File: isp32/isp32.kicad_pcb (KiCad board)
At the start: 2 copper layers, 58 parts, among them J1 BAT1, J3 USB_C_Receptacle_USB2.0, J6 F0, J7 F1, Q1 BSS138, Q2 BSS138, Q3 IRLML6402, Q4 BSS138, Q5 IRLML6402, Q6 S8050, Q7 S8050, Q8 S8050, U1 ICE40HX8K-BG121, U10 BMP280, U11 MPU-9250, U12 CH340C, U2 USBLC6-2SC6, U3 ESP32-WROOM-32U, U4 AMS1117-3.3, U5 MP2303ADN, U6 MIC5504-1.2YM5, U7 NEO-XM, U8 AT25SF081-SSHD-X, U9 RFM98W-315S2, X1 ASE-25MHz

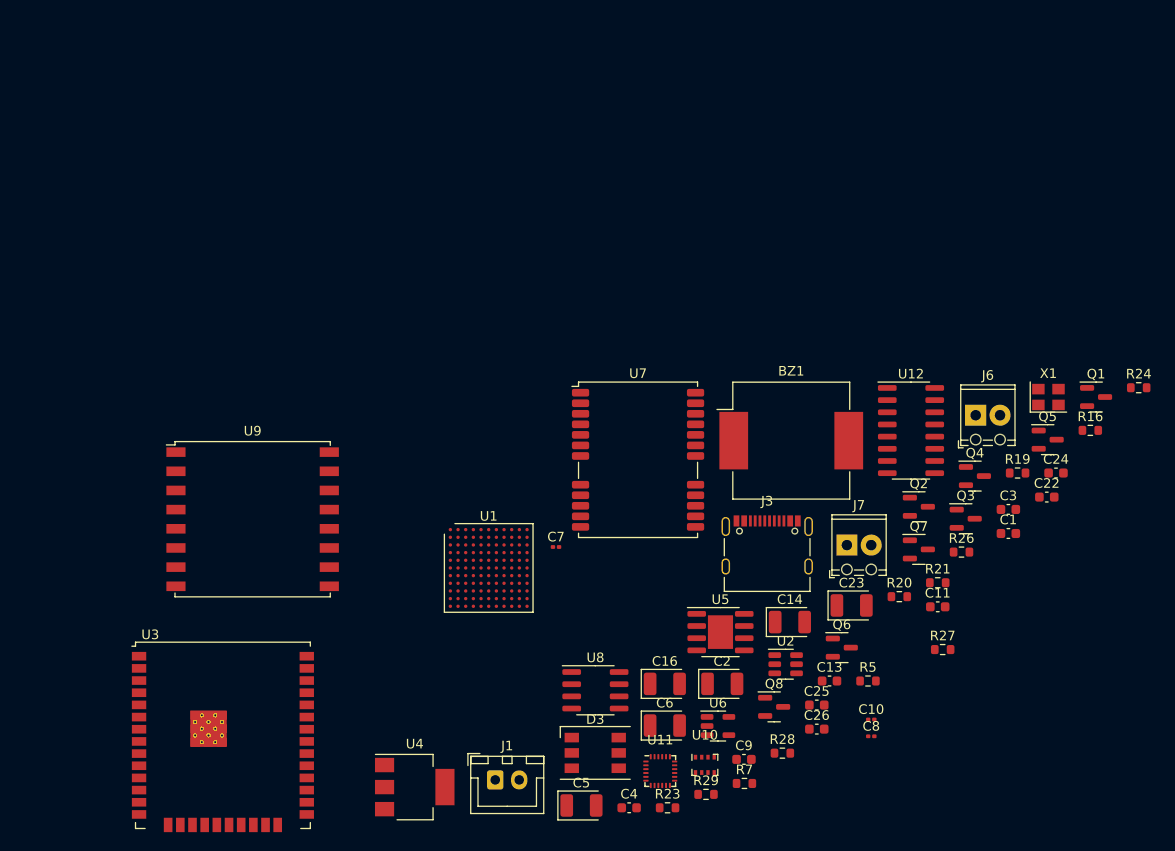
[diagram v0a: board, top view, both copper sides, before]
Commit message: Select isp32 footprint
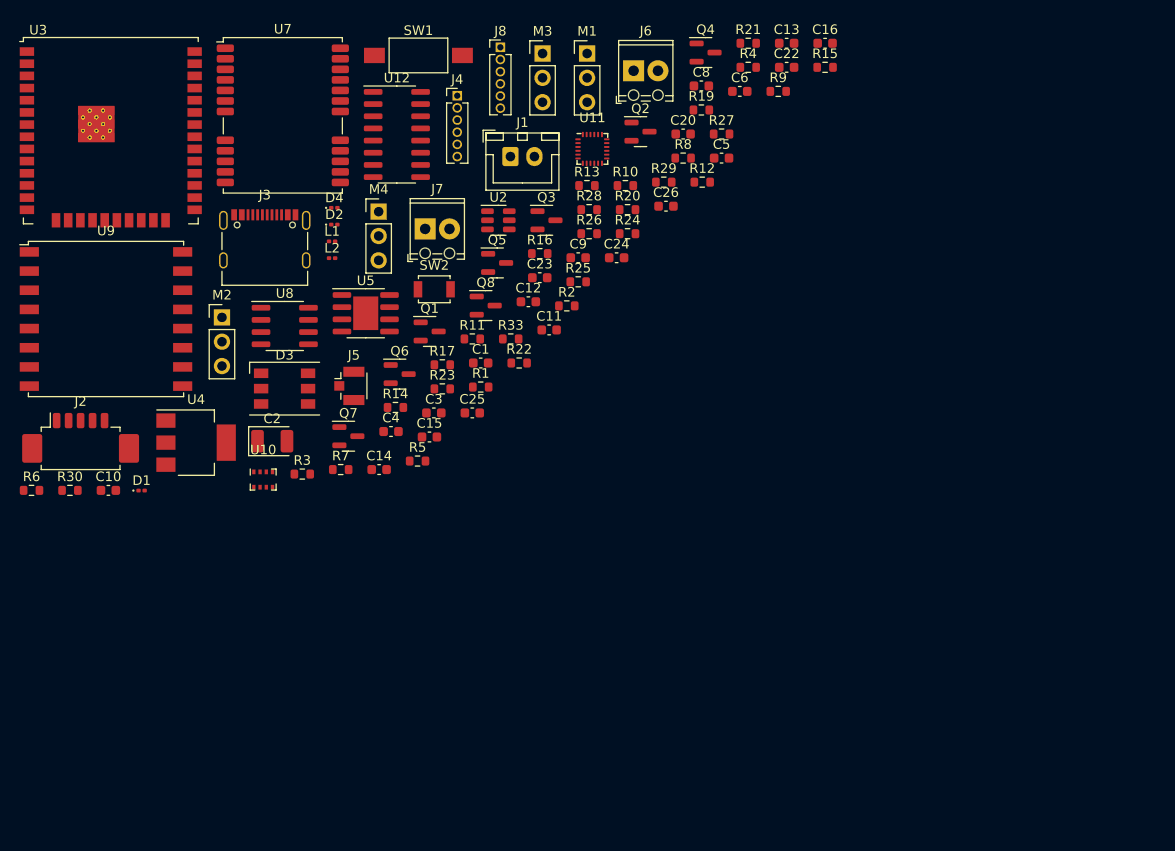
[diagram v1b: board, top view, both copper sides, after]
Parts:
- removed BZ1: Buzzer, Buzzer_Beeper:Buzzer_Mallory_AST1240MLQ
- removed C7: 1u, Capacitor_SMD:C_0201_0603Metric
- removed U1: ICE40HX8K-BG121, Package_BGA:BGA-121_9.0x9.0mm_Layout11x11_P0.8mm_Ball0.4mm_Pad0.35mm_NSMD
- removed U6: MIC5504-1.2YM5, Package_TO_SOT_SMD:SOT-23-5
- removed X1: ASE-25MHz, Oscillator:Oscillator_SMD_Abracon_ASE-4Pin_3.2x2.5mm
- added C12: 2.2n, Capacitor_SMD:C_0603_1608Metric, F.Cu at (109.2, 59.7)
- added C15: 47u, Capacitor_SMD:C_0603_1608Metric, F.Cu at (98.8, 73.8)
- added C20: 100n, Capacitor_SMD:C_0603_1608Metric, F.Cu at (125.3, 42.2)
- added D1: GPS_LED, LED_SMD:LED_0201_0603Metric, F.Cu at (68.8, 79.4)
- added D2: F0_LED, LED_SMD:LED_0201_0603Metric, F.Cu at (88.9, 51.7)
- added D4: F1_LED, LED_SMD:LED_0201_0603Metric, F.Cu at (88.9, 49.9)
- added J2: Switching, Connector_Molex:Molex_PicoBlade_53261-0571_1x05-1MP_P1.25mm_Horizontal, F.Cu at (62.5, 74.5)
- added J4: ESP_JTAG, Connector_PinHeader_1.27mm:PinHeader_1x06_P1.27mm_Vertical, F.Cu at (101.8, 38.2)
- added J5: GPS_ANT, Connector_Coaxial:U.FL_Hirose_U.FL-R-SMT-1_Vertical, F.Cu at (90.5, 68.5)
- added J8: Flash_SPI, Connector_PinHeader_1.27mm:PinHeader_1x06_P1.27mm_Vertical, F.Cu at (106.2, 33.2)
- added L1: 10u, Inductor_SMD:L_0201_0603Metric, F.Cu at (88.7, 53.4)
- added L2: 22u, Inductor_SMD:L_0201_0603Metric, F.Cu at (88.7, 55.2)
- added M1: Motor_Servo, Connector_PinHeader_2.54mm:PinHeader_1x03_P2.54mm_Vertical, F.Cu at (115.3, 33.8)
- added M2: Motor_Servo, Connector_PinHeader_2.54mm:PinHeader_1x03_P2.54mm_Vertical, F.Cu at (77.2, 61.3)
- added M3: Motor_Servo, Connector_PinHeader_2.54mm:PinHeader_1x03_P2.54mm_Vertical, F.Cu at (110.7, 33.8)
- added M4: Motor_Servo, Connector_PinHeader_2.54mm:PinHeader_1x03_P2.54mm_Vertical, F.Cu at (93.5, 50.3)
- added R1: 10k, Resistor_SMD:R_0603_1608Metric, F.Cu at (104.2, 68.6)
- added R10: 10k, Resistor_SMD:R_0603_1608Metric, F.Cu at (119.3, 47.6)
- added R11: 52.5k, Resistor_SMD:R_0603_1608Metric, F.Cu at (103.3, 63.6)
- added R12: 22, Resistor_SMD:R_0603_1608Metric, F.Cu at (127.3, 47.2)
- added R13: 330, Resistor_SMD:R_0603_1608Metric, F.Cu at (115.3, 47.6)
- added R14: 10k, Resistor_SMD:R_0603_1608Metric, F.Cu at (95.3, 70.7)
- added R15: 10k, Resistor_SMD:R_0603_1608Metric, F.Cu at (140.1, 35.2)
- added R17: 10k, Resistor_SMD:R_0603_1608Metric, F.Cu at (100.2, 66.3)
- added R2: 10k, Resistor_SMD:R_0603_1608Metric, F.Cu at (113.2, 60.1)
- added R22: 1k, Resistor_SMD:R_0603_1608Metric, F.Cu at (108.2, 66.1)
- added R25: 1k, Resistor_SMD:R_0603_1608Metric, F.Cu at (114.4, 57.6)
- added R3: 10k, Resistor_SMD:R_0603_1608Metric, F.Cu at (85.6, 77.7)
- added R30: 10k, Resistor_SMD:R_0603_1608Metric, F.Cu at (61.3, 79.4)
- added R33: 10k, Resistor_SMD:R_0603_1608Metric, F.Cu at (107.3, 63.6)
- added R4: 4k7, Resistor_SMD:R_0603_1608Metric, F.Cu at (132.1, 35.2)
- added R6: 4k7, Resistor_SMD:R_0603_1608Metric, F.Cu at (57.3, 79.4)
- added R8: 100k, Resistor_SMD:R_0603_1608Metric, F.Cu at (125.3, 44.7)
- added R9: 91k, Resistor_SMD:R_0603_1608Metric, F.Cu at (135.2, 37.8)
- added SW1: RST, Button_Switch_SMD:SW_SPST_FSMSM, F.Cu at (97.7, 34.0)
- added SW2: IO0, Button_Switch_SMD:SW_SPST_B3U-1000P, F.Cu at (99.3, 58.4)
- C10, C8: footprint Capacitor_SMD:C_0201_0603Metric -> Capacitor_SMD:C_0603_1608Metric
- C14, C16, C23, C5, C6: footprint Capacitor_Tantalum_SMD:CP_EIA-3528-12_Kemet-T -> Capacitor_SMD:C_0603_1608Metric
- moved C10 83.1 mm to (65.3, 79.4)
- moved C8 70.1 mm to (127.2, 37.2)
- moved Q1 69.9 mm to (98.9, 62.8)
- moved C5 69.1 mm to (129.3, 44.7)
- moved C16 68.9 mm to (140.1, 32.7)
- moved C13 66.7 mm to (136.1, 32.7)
- moved C6 66.6 mm to (131.2, 37.8)
- moved U11 65.3 mm to (115.8, 43.8)
- moved J1 65.1 mm to (107.3, 44.6)
- moved U3 64.2 mm to (65.6, 41.9)
- moved R29 64.0 mm to (123.3, 47.2)
- moved U12 61.9 mm to (95.5, 42.3)
- moved J3 61.4 mm to (81.7, 53.1)
- moved C3 60.8 mm to (99.3, 71.3)
- moved Q7 60.7 mm to (90.4, 73.7)
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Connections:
- U12 pad 5: PS_D+ -> D+
- U12 pad 6: PS_D- -> D-

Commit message: Rough layout
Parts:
- removed C3: 10u, Capacitor_SMD:C_0603_1608Metric
- removed M1, M2, M3, M4: Motor_Servo, Connector_PinHeader_2.54mm:PinHeader_1x03_P2.54mm_Vertical
- added AE1: Antenna, Connector_PinHeader_2.00mm:PinHeader_1x01_P2.00mm_Vertical, B.Cu at (94.0, 85.0)
- added BZ1: Buzzer, Buzzer_Beeper:Buzzer_CUI_CPT-9019S-SMT, F.Cu at (88.0, 55.5)
- added D5: POWER, LED_SMD:LED_0603_1608Metric, F.Cu at (91.0, 46.0)
- added J9: Conn_01x12, Connector_PinHeader_2.54mm:PinHeader_1x12_P2.54mm_Horizontal, F.Cu at (118.5, 40.4)
- added R18: 1k, Resistor_SMD:R_0603_1608Metric, F.Cu at (94.3, 46.0)
- added REF**: MountingHole_3.2mm_M3_DIN965, MountingHole:MountingHole_3.2mm_M3_DIN965, F.Cu at (75.9, 34.4)
- added REF**: MountingHole_3.2mm_M3_DIN965, MountingHole:MountingHole_3.2mm_M3_DIN965, F.Cu at (118.4, 83.9)
- added REF**: MountingHole_3.2mm_M3_DIN965, MountingHole:MountingHole_3.2mm_M3_DIN965, F.Cu at (118.4, 34.4)
- added REF**: MountingHole_3.2mm_M3_DIN965, MountingHole:MountingHole_3.2mm_M3_DIN965, F.Cu at (75.9, 83.9)
- C10, C12, C15, C2, C20, C8, J2, R10, R11, R15, R30, R4, R6, R8, R9, U3, U5, U8, U9: moved to B.Cu
- C5: footprint Capacitor_SMD:C_0603_1608Metric -> Capacitor_SMD:C_0805_2012Metric; moved to B.Cu
- D1, D2, D4: footprint LED_SMD:LED_0201_0603Metric -> LED_SMD:LED_0603_1608Metric
- J1: footprint Connector_JST:JST_XH_B2B-XH-A_1x02_P2.50mm_Vertical -> Connector_AMASS:AMASS_XT60-M_1x02_P7.20mm_Vertical
- L1: footprint Inductor_SMD:L_0201_0603Metric -> Inductor_SMD:L_Abracon_ASPI-0630LR; moved to B.Cu
- L2: footprint Inductor_SMD:L_0201_0603Metric -> Inductor_SMD:L_0805_2012Metric
- R22, R25: value 1k -> 10k
- moved R9 61.9 mm to (75.5, 53.9), turned to -90 degrees
- moved J6 60.8 mm to (74.9, 76.2), turned to -90 degrees
- moved R30 60.4 mm to (110.1, 43.7)
- moved C22 60.2 mm to (81.0, 59.5), turned to 90 degrees
- moved Q4 59.7 mm to (80.6, 70.5), turned to 180 degrees
- moved R15 58.6 mm to (87.9, 61.9), turned to -90 degrees
- moved R21 57.9 mm to (75.9, 46.5), turned to 90 degrees
- moved C6 56.2 mm to (86.9, 72.2), turned to 180 degrees
- moved R4 53.8 mm to (99.5, 78.1)
- moved R8 49.9 mm to (75.5, 47.6), turned to -90 degrees
- moved C8 49.6 mm to (78.3, 45.4)
- moved R19 46.1 mm to (81.6, 46.3), turned to 90 degrees
- moved C13 45.7 mm to (100.7, 61.7), turned to 90 degrees
- moved R6 45.5 mm to (102.8, 78.1), turned to 180 degrees
- moved U3 45.0 mm to (105.4, 62.9)
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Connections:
- J2 pad 5: SCL -> SDA
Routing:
- net +3V3: track 0.00 -> 99.5 mm
- net +5V: track 0.00 -> 29.9 mm
- net +BATT: track 0.00 -> 27.5 mm, vias 0 -> 1
- net Net-(L1-Pad1): track 0.00 -> 14.4 mm
- net Net-(Q8-Pad1): track 0.00 -> 11.6 mm
- net cc1: track 0.00 -> 9.40 mm
- net Net-(Q7-Pad1): track 0.00 -> 9.37 mm
- net Net-(J6-Pad1): track 0.00 -> 8.88 mm
- net Net-(J7-Pad1): track 0.00 -> 8.70 mm
- net cc2: track 0.00 -> 8.50 mm
- net GND: track 0.00 -> 7.72 mm
- net Net-(J5-Pad1): track 0.00 -> 6.85 mm
- net Net-(Q8-Pad2): track 0.00 -> 6.50 mm
- net Net-(C10-Pad1): track 0.00 -> 5.81 mm
- net Net-(J3-PadA6): track 0.00 -> 5.75 mm
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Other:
- board outline added: 48.5 x 55.5 mm

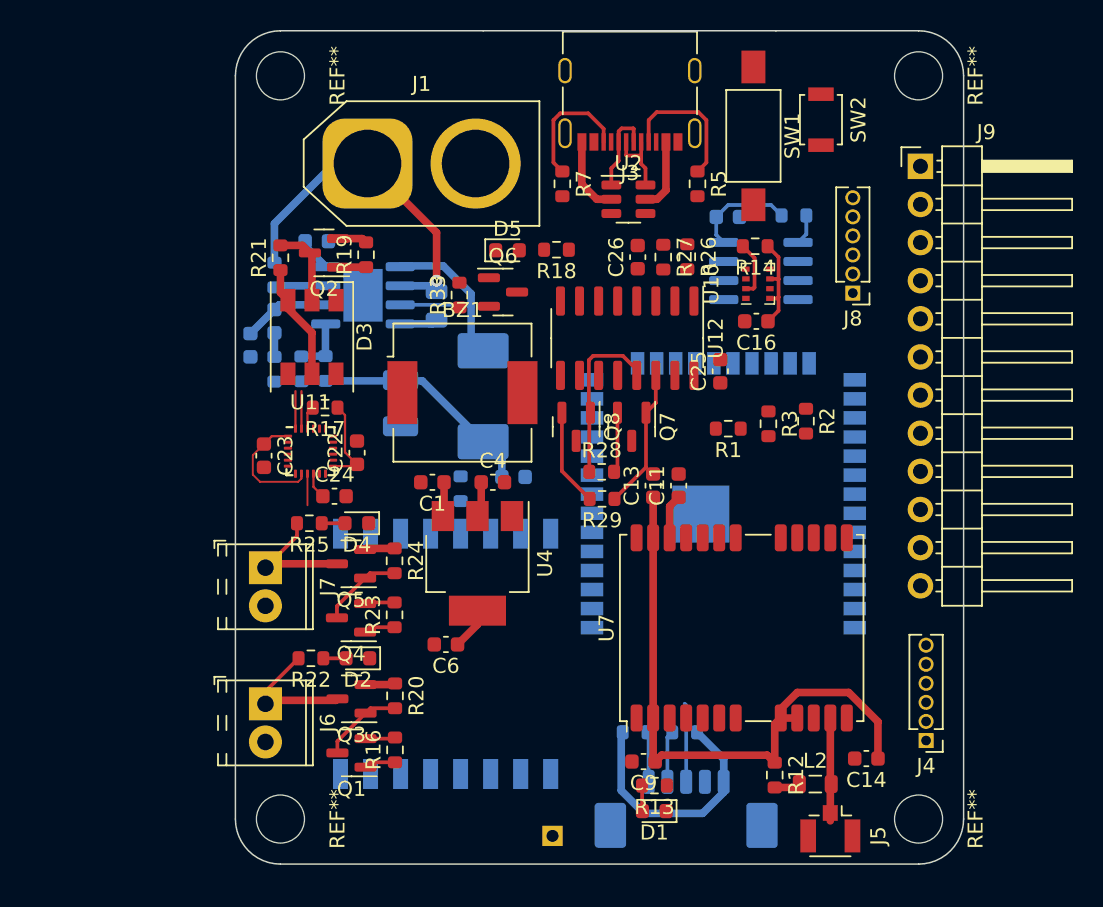
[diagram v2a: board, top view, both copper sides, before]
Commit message: Add logo and modify layout
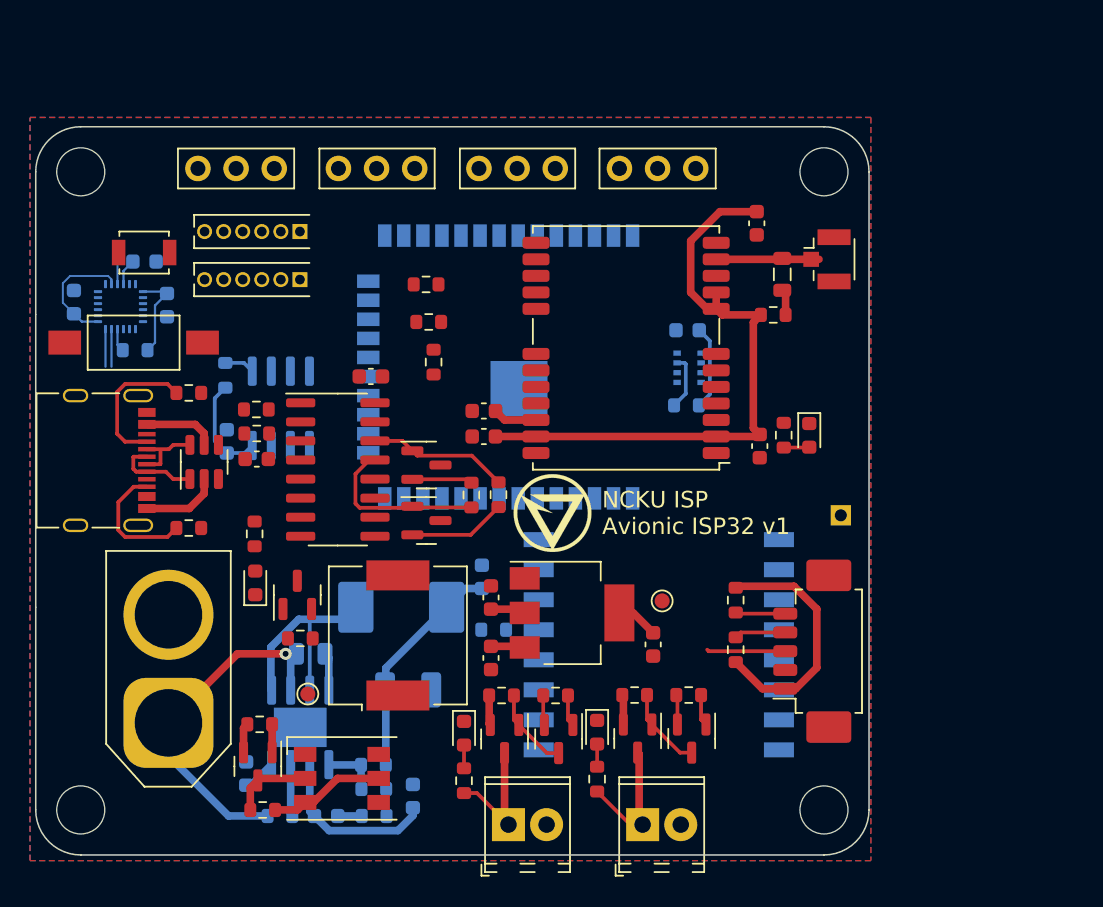
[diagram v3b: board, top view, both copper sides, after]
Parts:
- removed J9: Conn_01x12, Connector_PinHeader_2.54mm:PinHeader_1x12_P2.54mm_Horizontal
- added G***: LOGO, isp_logo:isp_logo, F.Cu at (94.0, 63.5)
- added M1: Motor_Servo, Connector_PinHeader_2.54mm:PinHeader_1x03_P2.54mm_Vertical, F.Cu at (70.4, 40.5)
- added M2: Motor_Servo, Connector_PinHeader_2.54mm:PinHeader_1x03_P2.54mm_Vertical, F.Cu at (79.7, 40.5)
- added M3: Motor_Servo, Connector_PinHeader_2.54mm:PinHeader_1x03_P2.54mm_Vertical, F.Cu at (89.1, 40.5)
- added M4: Motor_Servo, Connector_PinHeader_2.54mm:PinHeader_1x03_P2.54mm_Vertical, F.Cu at (98.5, 40.5)
- added TP1: TP3v3, TestPoint:TestPoint_Pad_D1.0mm, F.Cu at (101.3, 69.3)
- added TP2: TP5v, TestPoint:TestPoint_Pad_D1.0mm, F.Cu at (77.7, 75.5)
- C16, C22, C23, C24, R14, R17, U10, U11: moved to B.Cu
- J2, R4, R6: moved to F.Cu
- moved REF** 56.2 mm to (62.6, 40.8), turned to 0 degrees
- moved J4 53.7 mm to (77.2, 44.8), turned to -90 degrees
- moved REF** 50.7 mm to (62.6, 83.3), turned to 0 degrees
- moved SW2 45.9 mm to (66.8, 46.1), turned to 0 degrees
- moved REF** 43.6 mm to (112.1, 40.8), turned to 0 degrees
- moved SW1 43.5 mm to (66.1, 52.1), turned to 0 degrees
- moved J3 42.0 mm to (64.5, 60.0), turned to -90 degrees
- moved J1 39.5 mm to (68.4, 77.5), turned to 90 degrees
- moved R30 39.3 mm to (72.2, 54.3), turned to 90 degrees
- moved J5 37.9 mm to (112.3, 46.6), turned to 0 degrees
- moved J8 36.8 mm to (77.2, 48.0), turned to -90 degrees
- moved R21 36.8 mm to (74.7, 83.3), turned to 180 degrees
- moved R5 36.6 mm to (69.8, 55.5), turned to 0 degrees
- moved C20 36.6 mm to (72.3, 58.7), turned to 90 degrees
- moved C14 36.4 mm to (107.6, 44.2), turned to -90 degrees
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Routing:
- net Net-(C10-Pad1): track 5.81 -> 11.4 mm
- added copper zone on B.Cu, net GND
- added copper zone on F.Cu, net GND
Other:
- board size 48.5 x 55.5 mm -> 55.5 x 48.5 mm
- board text added: "NCKU ISP Avionic ISP32 v1"
